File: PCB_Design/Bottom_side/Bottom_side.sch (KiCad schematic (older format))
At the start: 2 parts

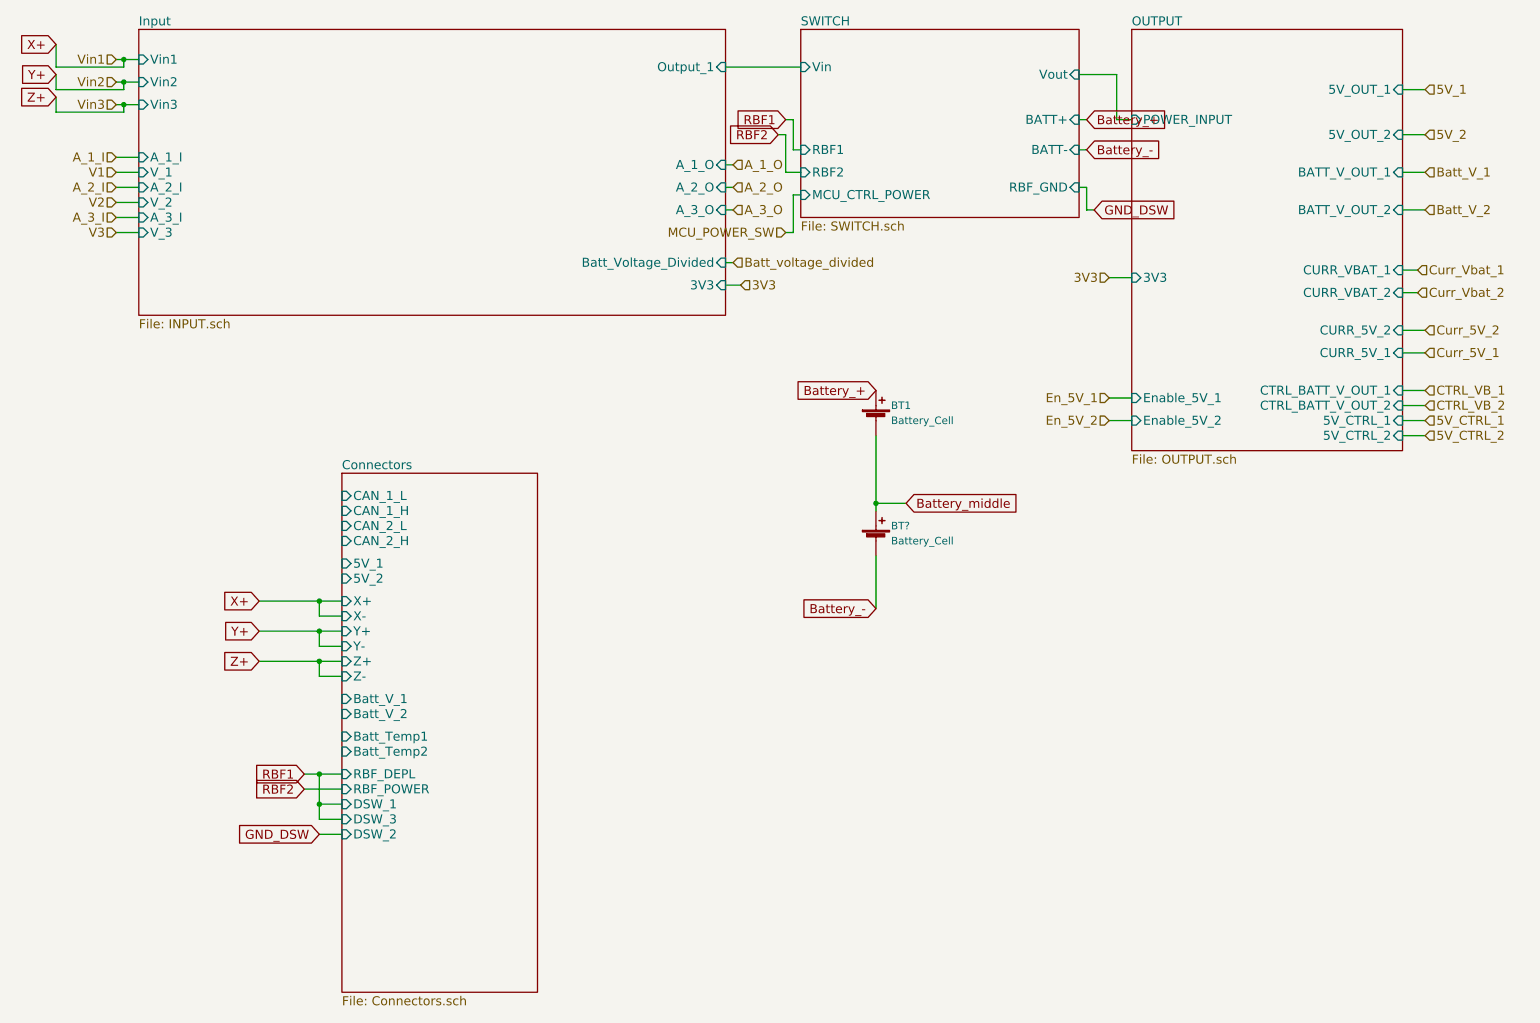
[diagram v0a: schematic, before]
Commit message: PCB bottom layer populated
PCB bottom layer populated, and waiting for top layer to be merged.
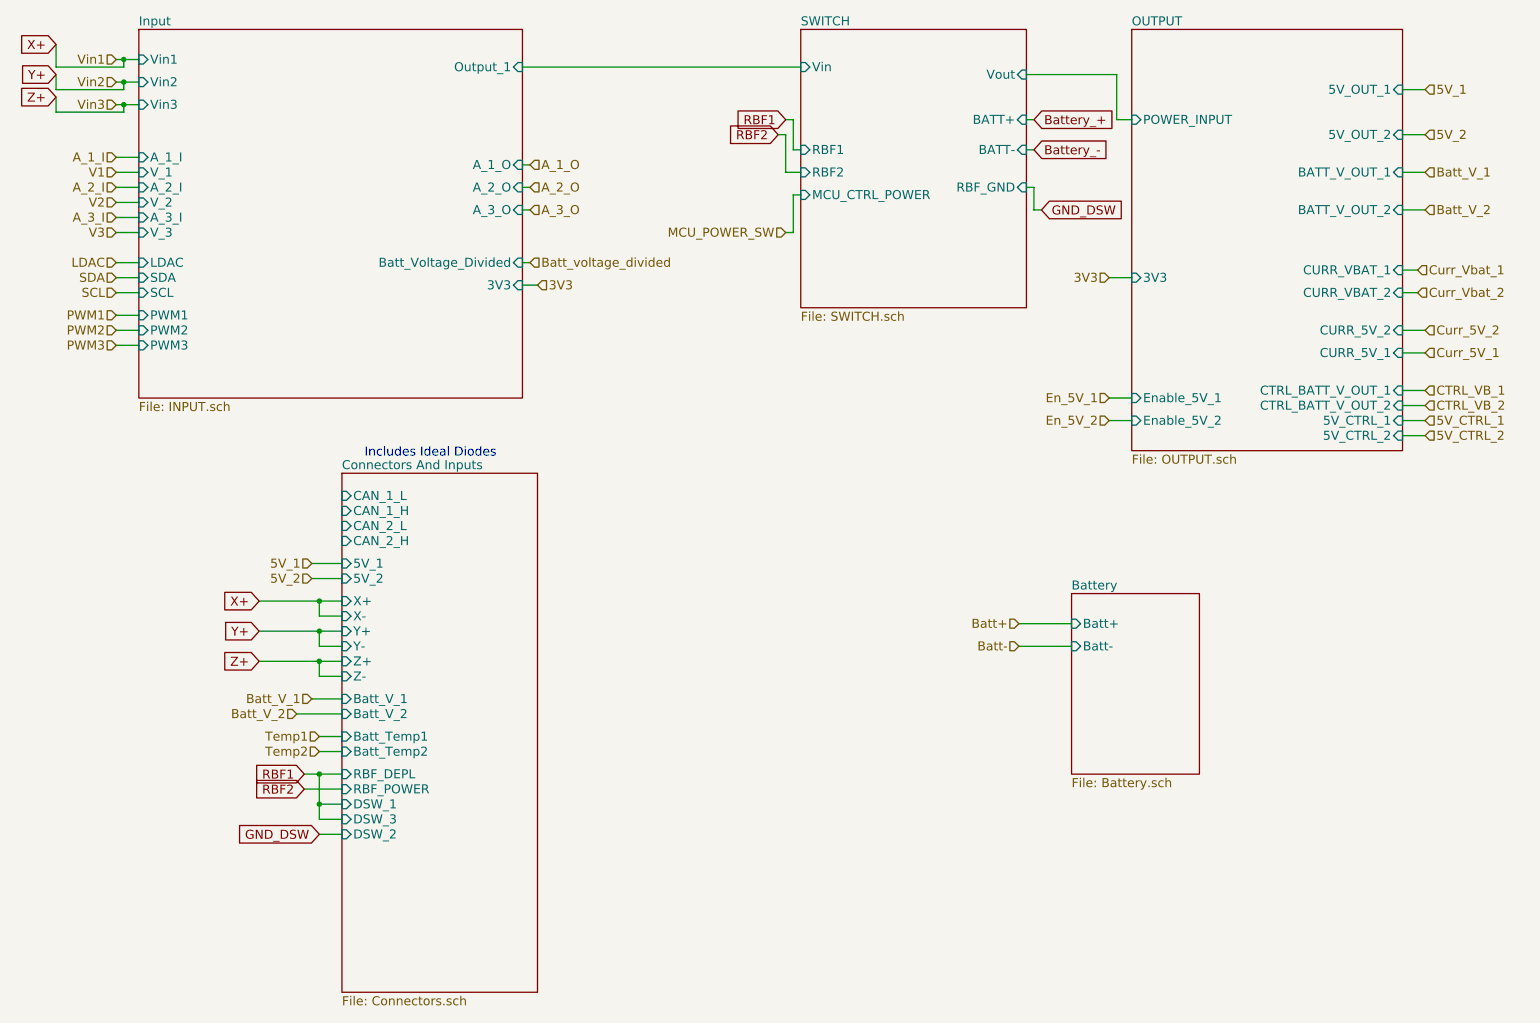
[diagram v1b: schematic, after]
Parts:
- removed BT1, BT?: Battery_Cell, Batt_Hold:18650_Holder, symbol Battery_Cell
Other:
- note added: "Includes Ideal Diodes"
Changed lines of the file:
@@
 LIBS:contrib
 LIBS:valves
-LIBS:Custom_Library
 LIBS:Bottom_side-cache
 EELAYER 25 0
@@
 $Descr A4 11693 8268
 encoding utf-8
-Sheet 1 25
+Sheet 1 26
 Title ""
 Date ""
@@
 $EndDescr
 $Sheet
-S 1250 1200 3900 1900
+S 1250 1200 2550 2450
 U 5A57B48D
 F0 "Input" 60
@@
 F9 "Vin2" I L 1250 1550 60
 F10 "Vin3" I L 1250 1700 60
-F11 "A_1_O" I R 5150 2100 60
-F12 "A_2_O" I R 5150 2250 60
-F13 "A_3_O" I R 5150 2400 60
-F14 "Output_1" I R 5150 1450 60
-F15 "3V3" I R 5150 2900 60
-F16 "Batt_Voltage_Divided" I R 5150 2750 60
+F11 "A_1_O" I R 3800 2100 60
+F12 "A_2_O" I R 3800 2250 60
+F13 "A_3_O" I R 3800 2400 60
+F14 "Output_1" I R 3800 1450 60
+F15 "3V3" I R 3800 2900 60
+F16 "Batt_Voltage_Divided" I R 3800 2750 60
+F17 "LDAC" I L 1250 2750 60
+F18 "SDA" I L 1250 2850 60
+F19 "SCL" I L 1250 2950 60
+F20 "PWM1" I L 1250 3100 60
+F21 "PWM2" I L 1250 3200 60
+F22 "PWM3" I L 1250 3300 60
 $EndSheet
 $Sheet
-S 5650 1200 1850 1250
+S 5650 1200 1500 1850
 U 5A57B544
 F0 "SWITCH" 60
@@
 F4 "RBF2" I L 5650 2150 60
 F5 "MCU_CTRL_POWER" I L 5650 2300 60
-F6 "Vout" I R 7500 1500 60
-F7 "BATT+" I R 7500 1800 60
-F8 "BATT-" I R 7500 2000 60
-F9 "RBF_GND" I R 7500 2250 60
+F6 "Vout" I R 7150 1500 60
+F7 "BATT+" I R 7150 1800 60
+F8 "BATT-" I R 7150 2000 60
+F9 "RBF_GND" I R 7150 2250 60
 $EndSheet
 $Sheet
@@
 Text HLabel 1100 2550 0    60   Input ~ 0
 V3
-Text HLabel 5200 2100 2    60   Input ~ 0
+Text HLabel 3850 2100 2    60   Input ~ 0
 A_1_O
-Text HLabel 5200 2250 2    60   Input ~ 0
+Text HLabel 3850 2250 2    60   Input ~ 0
 A_2_O
-Text HLabel 5200 2400 2    60   Input ~ 0
+Text HLabel 3850 2400 2    60   Input ~ 0
 A_3_O
-Text HLabel 5200 2750 2    60   Input ~ 0
+Text HLabel 3850 2750 2    60   Input ~ 0
 Batt_voltage_divided
-Text HLabel 5250 2900 2    60   Input ~ 0
+Text HLabel 3900 2900 2    60   Input ~ 0
 3V3
 Wire Wire Line
@@
 	1100 1400 1250 1400
 Wire Wire Line
-	5150 1450 5650 1450
-Wire Wire Line
-	5200 2100 5150 2100
-Wire Wire Line
-	5200 2250 5150 2250
-Wire Wire Line
-	5150 2400 5200 2400
-Wire Wire Line
-	5150 2750 5200 2750
-Wire Wire Line
-	5150 2900 5250 2900
+	3800 1450 5650 1450
+Wire Wire Line
+	3850 2100 3800 2100
+Wire Wire Line
+	3850 2250 3800 2250
+Wire Wire Line
+	3800 2400 3850 2400
+Wire Wire Line
+	3800 2750 3850 2750
+Wire Wire Line
+	3800 2900 3900 2900
 Wire Wire Line
 	5650 2000 5600 2000
@@
 	5600 2300 5650 2300
 Wire Wire Line
-	7500 1500 7750 1500
-Wire Wire Line
-	7750 1500 7750 1800
-Wire Wire Line
-	7750 1800 7850 1800
-Wire Wire Line
-	7550 1800 7500 1800
-Wire Wire Line
-	7500 2000 7550 2000
-Wire Wire Line
-	7600 2400 7550 2400
-Wire Wire Line
-	7550 2400 7550 2250
-Wire Wire Line
-	7550 2250 7500 2250
+	7150 1500 7750 1500
+Wire Wire Line
+	7200 1800 7150 1800
+Wire Wire Line
+	7150 2000 7200 2000
+Wire Wire Line
+	7250 2400 7200 2400
+Wire Wire Line
+	7200 2400 7200 2250
+Wire Wire Line
+	7200 2250 7150 2250
 Text HLabel 9800 1600 2    60   Input ~ 0
 5V_1
@@
 Text HLabel 9800 2150 2    60   Input ~ 0
 Batt_V_1
-Text HLabel 9800 2400 2    60   Input ~ 0
-Batt_V_2
 Text HLabel 9750 2800 2    60   Input ~ 0
 Curr_Vbat_1
@@
 S 2600 4150 1300 3450
 U 5A6B2220
-F0 "Connectors" 60
+F0 "Connectors And Inputs" 60
 F1 "Connectors.sch" 60
 F2 "CAN_1_L" I L 2600 4300 60
@@
 Text GLabel 2450 6550 0    60   Input ~ 0
 GND_DSW
-Text GLabel 7600 2400 2    60   Input ~ 0
+Text GLabel 7250 2400 2    60   Input ~ 0
 GND_DSW
 Wire Wire Line
@@
 	2450 5500 2450 5400
 Connection ~ 2450 5400
-$Comp
-L Battery_Cell BT1
-U 1 1 5A6ADD82
-P 6150 3800
-F 0 "BT1" H 6250 3900 50  0000 L CNN
-F 1 "Battery_Cell" H 6250 3800 50  0000 L CNN
-F 2 "Batt_Hold:18650_Holder" V 6150 3860 50  0001 C CNN
-F 3 "" V 6150 3860 50  0001 C CNN
-	1    6150 3800
-	1    0    0    -1
-$EndComp
-Wire Wire Line
-	6150 4700 6150 5050
-Wire Wire Line
-	6150 3900 6150 4400
-Wire Wire Line
-	6150 4350 6350 4350
-Connection ~ 6150 4350
-Text GLabel 6150 3600 0    60   Input ~ 0
+Text GLabel 7200 1800 2    60   Input ~ 0
 Battery_+
-Text GLabel 6150 5050 0    60   Input ~ 0
+Text GLabel 7200 2000 2    60   Input ~ 0
 Battery_-
-Text GLabel 6350 4350 2    60   Input ~ 0
-Battery_middle
-Text GLabel 7550 1800 2    60   Input ~ 0
-Battery_+
-Text GLabel 7550 2000 2    60   Input ~ 0
-Battery_-
-$Comp
-L Battery_Cell BT?
-U 1 1 5A70F7D2
-P 6150 4600
-F 0 "BT?" H 6250 4700 50  0000 L CNN
-F 1 "Battery_Cell" H 6250 4600 50  0000 L CNN
-F 2 "Batt_Hold:18650_Holder" V 6150 4660 50  0001 C CNN
-F 3 "" V 6150 4660 50  0001 C CNN
-	1    6150 4600
-	1    0    0    -1
-$EndComp
+Text Notes 2750 4050 0    60   ~ 0
+Includes Ideal Diodes
+Text HLabel 2400 4750 0    60   Input ~ 0
+5V_1
+Wire Wire Line
+	2400 4750 2600 4750
+Wire Wire Line
+	2600 4850 2400 4850
+Text HLabel 2400 4850 0    60   Input ~ 0
+5V_2
+Text HLabel 2400 5650 0    60   Input ~ 0
+Batt_V_1
+Text HLabel 2300 5750 0    60   Input ~ 0
+Batt_V_2
+Wire Wire Line
+	2400 5650 2600 5650
+Wire Wire Line
+	2300 5750 2600 5750
+Text HLabel 9800 2400 2    60   Input ~ 0
+Batt_V_2
+$Sheet
+S 7450 4950 850  1200
+U 5A77F4E8
+F0 "Battery" 60
+F1 "Battery.sch" 60
+F2 "Batt+" I L 7450 5150 60
+F3 "Batt-" I L 7450 5300 60
+$EndSheet
+Text HLabel 1100 2750 0    60   Input ~ 0
+LDAC
+Text HLabel 1100 2850 0    60   Input ~ 0
+SDA
+Text HLabel 1100 2950 0    60   Input ~ 0
+SCL
+Text HLabel 1100 3100 0    60   Input ~ 0
+PWM1
+Text HLabel 1100 3200 0    60   Input ~ 0
+PWM2
+Text HLabel 1100 3300 0    60   Input ~ 0
+PWM3
+Wire Wire Line
+	1100 2750 1250 2750
+Wire Wire Line
+	1250 2850 1100 2850
+Wire Wire Line
+	1100 2950 1250 2950
+Wire Wire Line
+	1250 3100 1100 3100
+Wire Wire Line
+	1100 3200 1250 3200
+Wire Wire Line
+	1250 3300 1100 3300
+Wire Wire Line
+	7750 1500 7750 1800
+Wire Wire Line
+	7750 1800 7850 1800
+Text HLabel 7100 5150 0    60   Input ~ 0
+Batt+
+Text HLabel 7100 5300 0    60   Input ~ 0
+Batt-
+Wire Wire Line
+	7100 5300 7450 5300
+Wire Wire Line
+	7450 5150 7100 5150
+Wire Wire Line
+	2600 5900 2450 5900
+Wire Wire Line
+	2600 6000 2450 6000
+Text HLabel 2450 5900 0    60   Input ~ 0
+Temp1
+Text HLabel 2450 6000 0    60   Input ~ 0
+Temp2
 $EndSCHEMATC
